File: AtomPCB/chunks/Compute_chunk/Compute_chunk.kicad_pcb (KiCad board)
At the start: 2 copper layers, 37 x 49 mm, 33 parts, among them J1 DF40C-40DP-0.4V_51_, U1 USBLC6-2SC6, U2 ESP32-S3-WROOM-1U-N8R8, U3 MPM3610AGQV-P, U4 SN74HCT125DR, U6 MPM3610AGQV-P

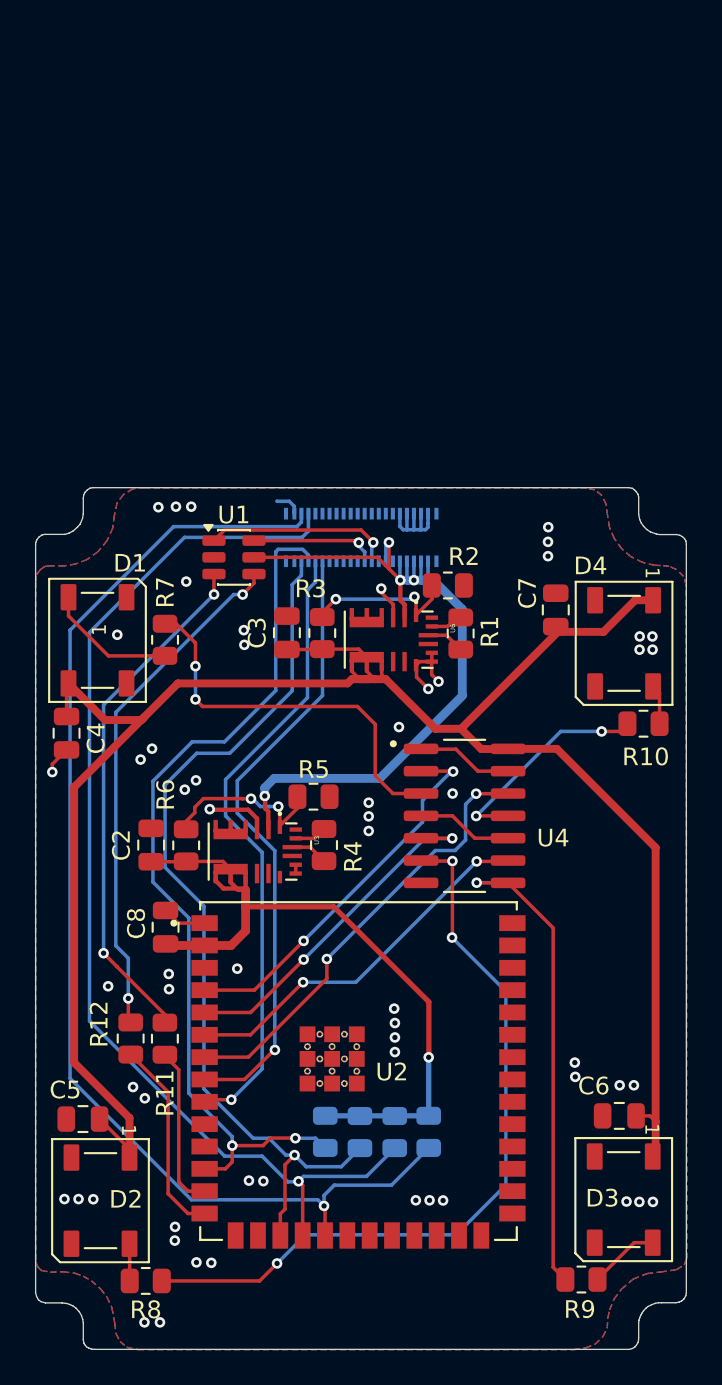
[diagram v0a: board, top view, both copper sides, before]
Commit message: updated compute chunk schematic to introduce missing resistor and capacitor. Changed diff resistor values on 3v3 buck
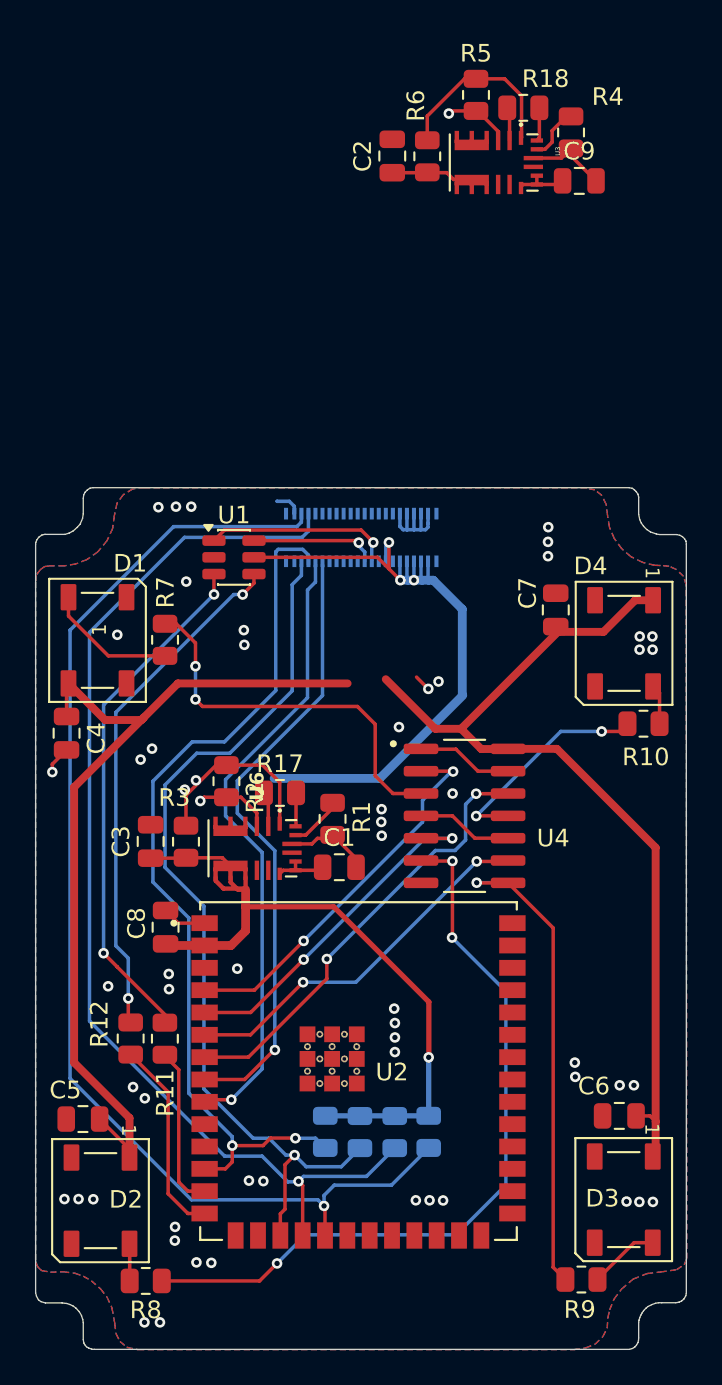
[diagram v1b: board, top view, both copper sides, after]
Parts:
- added C1: 10uF, Capacitor_SMD:C_0805_2012Metric, F.Cu at (128.8, 99.9)
- added C9: 10uF, Capacitor_SMD:C_0805_2012Metric, F.Cu at (142.4, 60.9)
- added R17: 100k, Resistor_SMD:R_0805_2012Metric, F.Cu at (125.4, 95.7)
- added R18: 100k, Resistor_SMD:R_0805_2012Metric, F.Cu at (139.2, 56.7)
- R2: value 20K -> 19.1k
- R3: value 105K -> 100k
- moved R4 42.9 mm to (141.9, 58.1)
- moved C2 41.5 mm to (131.8, 59.5)
- moved R6 41.5 mm to (133.8, 59.5)
- moved U3 41.5 mm to (137.6, 59.8)
- moved R5 41.0 mm to (136.5, 56.0), turned to 90 degrees
- moved R2 16.8 mm to (122.3, 95.0), turned to 90 degrees
- moved U6 14.2 mm to (123.8, 98.8)
- moved C3 14.2 mm to (118.0, 98.4)
- moved R3 14.2 mm to (120.0, 98.5)
- moved R1 12.8 mm to (128.4, 97.2)
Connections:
- R1 pad 1: VIN -> VBATT
- R4 pad 1: VIN -> VBATT
- U3 pad 16: VIN -> VBATT
- U3 pad 18: unconnected-(U3-PG-Pad18) -> Net-(U3-PG)
- U3 pad 2: VBATT -> 4.9V
- U6 pad 16: VIN -> VBATT
- U6 pad 18: unconnected-(U6-PG-Pad18) -> Net-(U6-PG)
- U6 pad 2: VBATT -> 4.9V
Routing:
- net 5.0V: track 112.9 -> 107.3 mm
- net GND: track 34.1 -> 39.1 mm
- net VBATT: track 43.4 -> 47.6 mm, vias 4 -> 3
- net VIN: track 4.15 -> 0.00 mm
- net 4.9V: track 0.00 -> 3.92 mm
- net Net-(U3-PG): track 0.00 -> 1.92 mm
- net Net-(U6-PG): track 0.00 -> 1.91 mm
- net Net-(U6-FB): track 9.04 -> 10.5 mm, vias 2 -> 0
- net Net-(U3-EN): track 1.83 -> 3.10 mm
- net Net-(U6-EN): track 1.85 -> 2.78 mm
- net Net-(U3-FB): track 9.93 -> 10.4 mm, vias 2 -> 0

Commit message: comput chunk updates, fixing buck converter issues
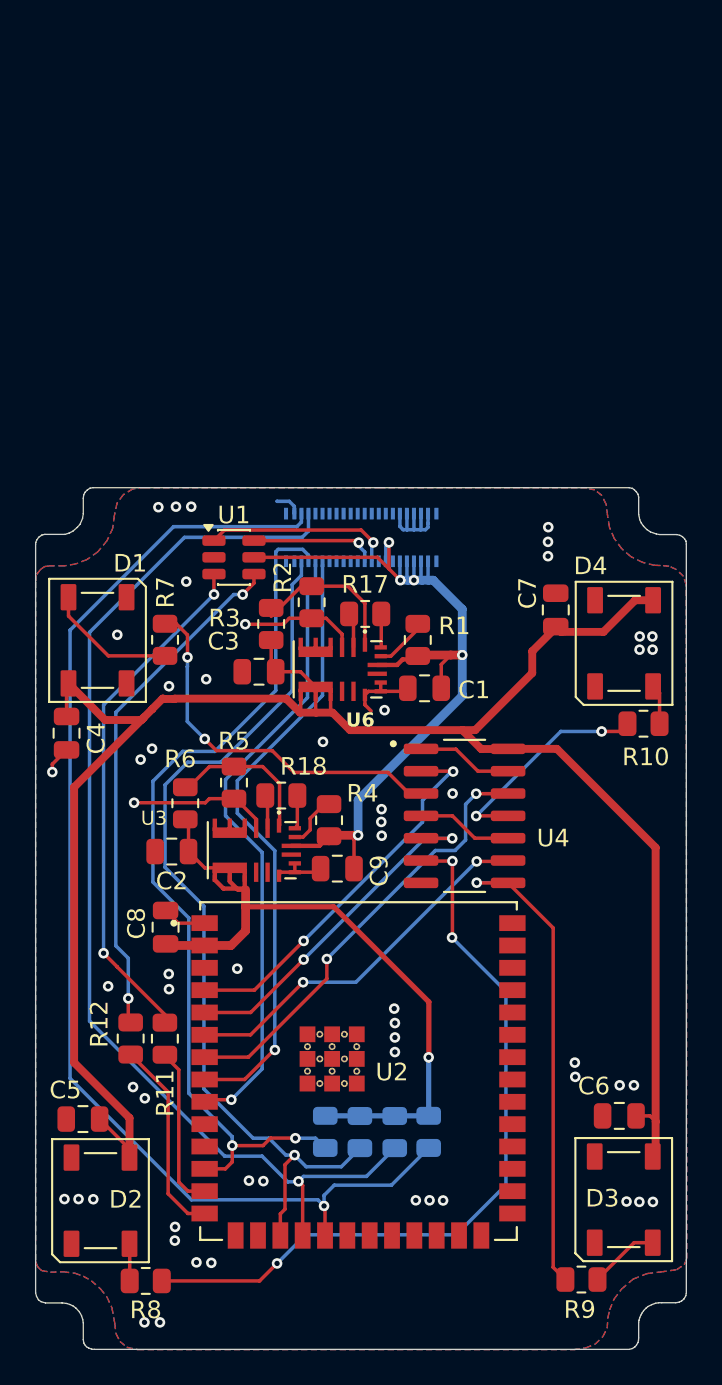
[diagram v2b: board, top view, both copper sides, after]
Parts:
- moved C2 41.5 mm to (119.2, 99.0), turned to 180 degrees
- moved C9 41.5 mm to (128.7, 100.0)
- moved R18 41.5 mm to (125.5, 95.8)
- moved R4 41.5 mm to (128.2, 97.2)
- moved R5 41.5 mm to (122.8, 95.1)
- moved U3 41.5 mm to (123.8, 98.9)
- moved R6 39.3 mm to (120.0, 96.3)
- moved R3 13.3 mm to (124.9, 86.1)
- moved C3 11.4 mm to (124.2, 88.8), turned to 180 degrees
- moved R17 11.3 mm to (130.2, 85.5)
- moved U6 11.3 mm to (128.7, 88.7)
- moved C1 11.3 mm to (133.6, 89.7)
- moved R1 11.3 mm to (133.2, 87.0)
- moved R2 11.3 mm to (127.2, 84.8)
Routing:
- net GND: track 39.1 -> 45.7 mm, vias 58 -> 55
- net 5.0V: track 107.3 -> 112.5 mm
- net Net-(U6-FB): track 10.5 -> 8.80 mm
- net Net-(U3-FB): track 10.4 -> 8.74 mm
- net VBATT: track 47.6 -> 49.3 mm, vias 3 -> 5
- net /LED1_CH: track 22.1 -> 21.4 mm
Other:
- board text added: "V0.2"
- board text removed: "V0.1"
